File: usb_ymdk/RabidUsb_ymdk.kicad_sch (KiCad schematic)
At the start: 16 parts, among them J1 USB_C_Receptacle_USB2.0, J2 Conn_01x04, U1 SRV05-4

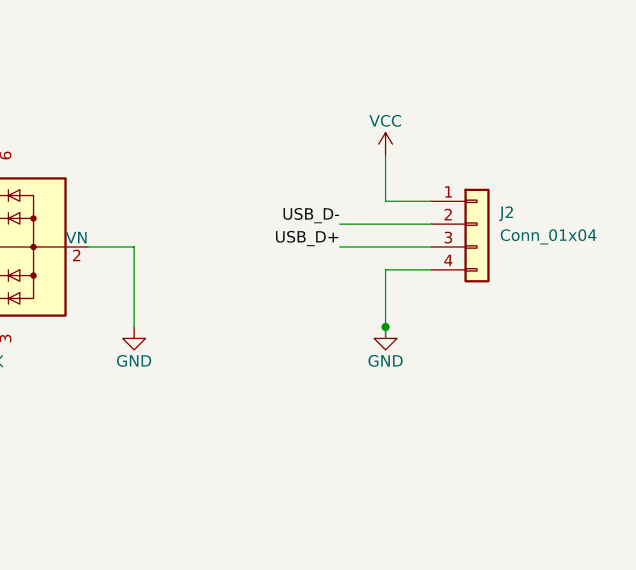
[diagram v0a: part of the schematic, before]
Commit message: USB: Add ferrite beads to YMDK USB board.
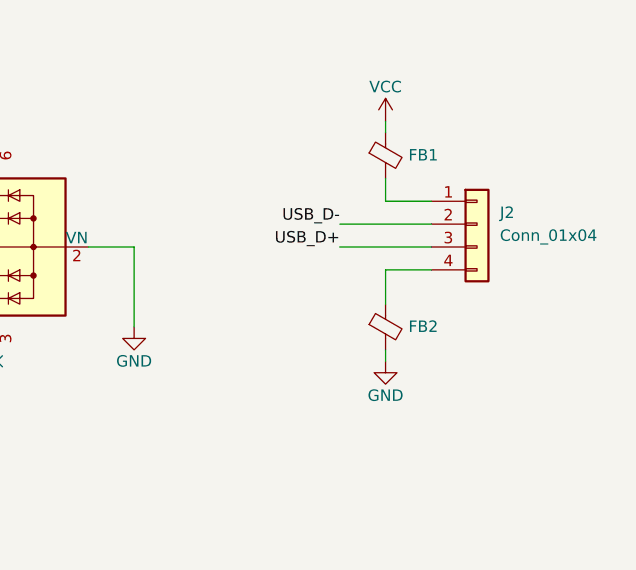
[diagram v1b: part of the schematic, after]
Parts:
- added FB1, FB2: FerriteBead_Small, Inductor_SMD:L_0805_2012Metric, symbol Device:FerriteBead_Small
- H1, H2, H3, H4: footprint ymdk_footprints:MountingHole_2.5mm_Pad_1mm -> ymdk_footprints:MountingHole_.12in_Pad_.02in
- J2: footprint Connector_PinHeader_2.00mm:PinHeader_1x04_P2.00mm_Vertical -> ymdk_footprints:PinHeader_1x04_P2.00mm_Fingers
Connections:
- net GND: now also FB2.2; no longer J2.4 (Pin_4)
- net VCC: now also FB1.1; no longer J2.1 (Pin_1)
- new net: FB1.2, J2.1 (Pin_1)
- new net: FB2.1, J2.4 (Pin_4)
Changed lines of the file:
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@@
   (junction (at 71.12 36.83) (diameter 0) (color 0 0 0 0)
-  )
-  (junction (at 172.72 54.61) (diameter 0) (color 0 0 0 0)
   )
   (no_connect (at 55.88 59.69))
@@
     (stroke (width 0) (type solid) (color 0 0 0 0))
   )
-  (wire (pts (xy 172.72 54.61) (xy 172.72 55.88))
-    (stroke (width 0) (type default) (color 0 0 0 0))
-  )
   (wire (pts (xy 104.14 45.72) (xy 114.3 45.72))
     (stroke (width 0) (type default) (color 0 0 0 0))
@@
     (stroke (width 0) (type solid) (color 0 0 0 0))
   )
-  (wire (pts (xy 172.72 35.56) (xy 172.72 40.64))
-    (stroke (width 0) (type default) (color 0 0 0 0))
-  )
   (wire (pts (xy 87.63 25.4) (xy 87.63 29.21))
     (stroke (width 0) (type default) (color 0 0 0 0))
@@
     (stroke (width 0) (type default) (color 0 0 0 0))
   )
+  (wire (pts (xy 172.72 48.26) (xy 172.72 52.07))
+    (stroke (width 0) (type default) (color 0 0 0 0))
+  )
   (polyline (pts (xy 25.4 130.81) (xy 113.03 130.81))
     (stroke (width 0) (type default) (color 0 0 0 0))
   )
+  (wire (pts (xy 172.72 38.1) (xy 172.72 40.64))
+    (stroke (width 0) (type default) (color 0 0 0 0))
+  )
   (wire (pts (xy 33.02 68.58) (xy 36.83 68.58))
     (stroke (width 0) (type solid) (color 0 0 0 0))
   )
+  (wire (pts (xy 172.72 31.75) (xy 172.72 33.02))
+    (stroke (width 0) (type default) (color 0 0 0 0))
+  )
   (wire (pts (xy 64.77 36.83) (xy 71.12 36.83))
     (stroke (width 0) (type solid) (color 0 0 0 0))
@@
     (stroke (width 0) (type default) (color 0 0 0 0))
   )
-  (wire (pts (xy 172.72 48.26) (xy 172.72 54.61))
-    (stroke (width 0) (type default) (color 0 0 0 0))
-  )
   (wire (pts (xy 167.64 45.72) (xy 177.8 45.72))
     (stroke (width 0) (type default) (color 0 0 0 0))
@@
   (wire (pts (xy 36.83 68.58) (xy 40.64 68.58))
     (stroke (width 0) (type solid) (color 0 0 0 0))
+  )
+  (wire (pts (xy 172.72 58.42) (xy 172.72 57.15))
+    (stroke (width 0) (type default) (color 0 0 0 0))
   )
   (wire (pts (xy 55.88 34.29) (xy 59.69 34.29))
@@
       (effects (font (size 1.27 1.27)) (justify left))
     )
-    (property "Footprint" "ymdk_footprints:MountingHole_2.5mm_Pad_1mm" (id 2) (at 35.56 107.95 0)
+    (property "Footprint" "ymdk_footprints:MountingHole_.12in_Pad_.02in" (id 2) (at 35.56 107.95 0)
       (effects (font (size 1.27 1.27)) hide)
     )
@@
       (effects (font (size 1.27 1.27)) (justify left))
     )
-    (property "Footprint" "ymdk_footprints:MountingHole_2.5mm_Pad_1mm" (id 2) (at 35.56 101.6 0)
+    (property "Footprint" "ymdk_footprints:MountingHole_.12in_Pad_.02in" (id 2) (at 35.56 101.6 0)
       (effects (font (size 1.27 1.27)) hide)
     )
@@
     )
   )
-  (symbol (lib_id "power:VCC") (at 172.72 35.56 0) (unit 1)
-    (in_bom yes) (on_board yes)
-    (property "Reference" "#PWR0107" (id 0) (at 172.72 39.37 0)
-      (effects (font (size 1.27 1.27)) hide)
-    )
-    (property "Value" "VCC" (id 1) (at 172.72 31.75 0))
-    (property "Footprint" "" (id 2) (at 172.72 35.56 0)
-      (effects (font (size 1.27 1.27)) hide)
-    )
-    (property "Datasheet" "" (id 3) (at 172.72 35.56 0)
+  (symbol (lib_id "power:VCC") (at 172.72 31.75 0) (unit 1)
+    (in_bom yes) (on_board yes)
+    (property "Reference" "#PWR0107" (id 0) (at 172.72 35.56 0)
+      (effects (font (size 1.27 1.27)) hide)
+    )
+    (property "Value" "VCC" (id 1) (at 172.72 27.94 0))
+    (property "Footprint" "" (id 2) (at 172.72 31.75 0)
+      (effects (font (size 1.27 1.27)) hide)
+    )
+    (property "Datasheet" "" (id 3) (at 172.72 31.75 0)
       (effects (font (size 1.27 1.27)) hide)
     )
@@
     (pin "6")
   )
+  (symbol (lib_id "Device:FerriteBead_Small") (at 172.72 35.56 0) (unit 1)
+    (in_bom yes) (on_board yes) (fields_autoplaced)
+    (property "Reference" "FB1" (id 0) (at 175.26 35.5218 0)
+      (effects (font (size 1.27 1.27)) (justify left))
+    )
+    (property "Value" "FerriteBead_Small" (id 1) (at 175.26 36.7918 0)
+      (effects (font (size 1.27 1.27)) (justify left) hide)
+    )
+    (property "Footprint" "Inductor_SMD:L_0805_2012Metric" (id 2) (at 170.942 35.56 90)
+      (effects (font (size 1.27 1.27)) hide)
+    )
+    (property "Datasheet" "https://datasheet.lcsc.com/lcsc/1811061723_FH-Guangdong-Fenghua-Advanced-Tech-CBW201209U301T_C67451.pdf" (id 3) (at 172.72 35.56 0)
+      (effects (font (size 1.27 1.27)) hide)
+    )
+    (property "LCSC" " C67451" (id 4) (at 172.72 35.56 0)
+      (effects (font (size 1.27 1.27)) hide)
+    )
+    (pin "1")
+    (pin "2")
+  )
   (symbol (lib_id "Mechanical:MountingHole_Pad") (at 35.56 95.25 270) (unit 1)
     (in_bom no) (on_board yes) (fields_autoplaced)
@@
       (effects (font (size 1.27 1.27)) (justify left))
     )
-    (property "Footprint" "ymdk_footprints:MountingHole_2.5mm_Pad_1mm" (id 2) (at 35.56 95.25 0)
+    (property "Footprint" "ymdk_footprints:MountingHole_.12in_Pad_.02in" (id 2) (at 35.56 95.25 0)
       (effects (font (size 1.27 1.27)) hide)
     )
@@
     (pin "1")
   )
-  (symbol (lib_id "power:GND") (at 172.72 54.61 0) (unit 1)
-    (in_bom yes) (on_board yes)
-    (property "Reference" "#PWR08" (id 0) (at 172.72 60.96 0)
-      (effects (font (size 1.27 1.27)) hide)
-    )
-    (property "Value" "GND" (id 1) (at 172.72 58.42 0))
-    (property "Footprint" "" (id 2) (at 172.72 54.61 0))
-    (property "Datasheet" "" (id 3) (at 172.72 54.61 0))
+  (symbol (lib_id "power:GND") (at 172.72 58.42 0) (unit 1)
+    (in_bom yes) (on_board yes)
+    (property "Reference" "#PWR08" (id 0) (at 172.72 64.77 0)
+      (effects (font (size 1.27 1.27)) hide)
+    )
+    (property "Value" "GND" (id 1) (at 172.72 62.23 0))
+    (property "Footprint" "" (id 2) (at 172.72 58.42 0))
+    (property "Datasheet" "" (id 3) (at 172.72 58.42 0))
     (pin "1")
   )
@@
       (effects (font (size 1.27 1.27)) (justify left))
     )
-    (property "Footprint" "Connector_PinHeader_2.00mm:PinHeader_1x04_P2.00mm_Vertical" (id 2) (at 182.88 43.18 0)
+    (property "Footprint" "ymdk_footprints:PinHeader_1x04_P2.00mm_Fingers" (id 2) (at 182.88 43.18 0)
       (effects (font (size 1.27 1.27)) hide)
     )
@@
     (pin "4")
   )
+  (symbol (lib_id "Device:FerriteBead_Small") (at 172.72 54.61 0) (unit 1)
+    (in_bom yes) (on_board yes) (fields_autoplaced)
+    (property "Reference" "FB2" (id 0) (at 175.26 54.5718 0)
+      (effects (font (size 1.27 1.27)) (justify left))
+    )
+    (property "Value" "FerriteBead_Small" (id 1) (at 175.26 55.8418 0)
+      (effects (font (size 1.27 1.27)) (justify left) hide)
+    )
+    (property "Footprint" "Inductor_SMD:L_0805_2012Metric" (id 2) (at 170.942 54.61 90)
+      (effects (font (size 1.27 1.27)) hide)
+    )
+    (property "Datasheet" "https://datasheet.lcsc.com/lcsc/1811061723_FH-Guangdong-Fenghua-Advanced-Tech-CBW201209U301T_C67451.pdf" (id 3) (at 172.72 54.61 0)
+      (effects (font (size 1.27 1.27)) hide)
+    )
+    (property "LCSC" " C67451" (id 4) (at 172.72 54.61 0)
+      (effects (font (size 1.27 1.27)) hide)
+    )
+    (pin "1")
+    (pin "2")
+  )
   (symbol (lib_id "Mechanical:Fiducial") (at 91.44 114.3 0) (unit 1)
     (in_bom no) (on_board yes) (fields_autoplaced)
@@
       (effects (font (size 1.27 1.27)) (justify left))
     )
-    (property "Footprint" "ymdk_footprints:MountingHole_2.5mm_Pad_1mm" (id 2) (at 35.56 114.3 0)
+    (property "Footprint" "ymdk_footprints:MountingHole_.12in_Pad_.02in" (id 2) (at 35.56 114.3 0)
       (effects (font (size 1.27 1.27)) hide)
     )
@@
       (reference "F1") (unit 1) (value "500mA") (footprint "Fuse:Fuse_1812_4532Metric")
     )
+    (path "/ce01c5ec-2682-47c5-a2d6-e61198cf1dd3"
+      (reference "FB1") (unit 1) (value "FerriteBead_Small") (footprint "Inductor_SMD:L_0805_2012Metric")
+    )
+    (path "/e6f7baf9-5c46-459b-b394-ac882b59e924"
+      (reference "FB2") (unit 1) (value "FerriteBead_Small") (footprint "Inductor_SMD:L_0805_2012Metric")
+    )
     (path "/732031ed-0f98-4524-ab12-56a5343cf649"
       (reference "FID1") (unit 1) (value "Fiducial") (footprint "Fiducial:Fiducial_1mm_Mask2mm")
@@
     )
     (path "/d3fab48d-7f83-4ccb-b45d-c8af9686aeaa"
-      (reference "H1") (unit 1) (value "MountingHole") (footprint "ymdk_footprints:MountingHole_2.5mm_Pad_1mm")
+      (reference "H1") (unit 1) (value "MountingHole") (footprint "ymdk_footprints:MountingHole_.12in_Pad_.02in")
     )
     (path "/94ad9e63-55eb-4b2f-b9d9-a7a3aa251f57"
-      (reference "H2") (unit 1) (value "MountingHole") (footprint "ymdk_footprints:MountingHole_2.5mm_Pad_1mm")
+      (reference "H2") (unit 1) (value "MountingHole") (footprint "ymdk_footprints:MountingHole_.12in_Pad_.02in")
     )
     (path "/56f2f85a-8e48-4882-85e3-64d6dee0f85e"
-      (reference "H3") (unit 1) (value "MountingHole") (footprint "ymdk_footprints:MountingHole_2.5mm_Pad_1mm")
+      (reference "H3") (unit 1) (value "MountingHole") (footprint "ymdk_footprints:MountingHole_.12in_Pad_.02in")
     )
     (path "/f4c9da6e-7d52-42ff-b75b-8544ac893aa5"
-      (reference "H4") (unit 1) (value "MountingHole") (footprint "ymdk_footprints:MountingHole_2.5mm_Pad_1mm")
+      (reference "H4") (unit 1) (value "MountingHole") (footprint "ymdk_footprints:MountingHole_.12in_Pad_.02in")
     )
     (path "/c13f61be-60de-49fc-b1a6-9086577228b1"
@@
     )
     (path "/db81c6c3-e89b-4177-bf13-eb2a692cc076"
-      (reference "J2") (unit 1) (value "Conn_01x04") (footprint "Connector_PinHeader_2.00mm:PinHeader_1x04_P2.00mm_Vertical")
+      (reference "J2") (unit 1) (value "Conn_01x04") (footprint "ymdk_footprints:PinHeader_1x04_P2.00mm_Fingers")
     )
     (path "/6402d117-4099-4f7a-96cd-cc834ee226c2"
